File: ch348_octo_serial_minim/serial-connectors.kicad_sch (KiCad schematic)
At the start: 2 parts, among them J15 Conn_01x04

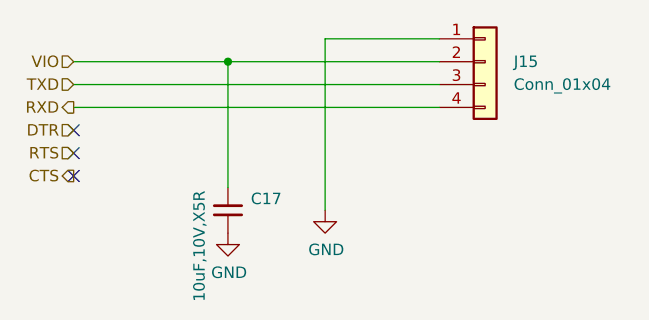
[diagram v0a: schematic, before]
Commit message: ch348_octo_serial_minim: jan2023 rev ready for production
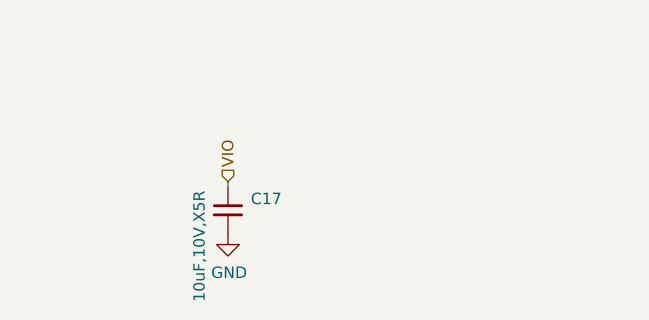
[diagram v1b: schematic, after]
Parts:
- removed J15: Conn_01x04, tom-connectors:PinHeader_1x04_P2.54mm_Vertical, symbol tom-connectors:Conn_01x04
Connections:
- no-connect marks 3 -> 0
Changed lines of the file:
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@@
 (kicad_sch (version 20211123) (generator eeschema)
   (paper "A4")
-  (junction (at 67.31 69.215) (diameter 0) (color 0 0 0 0)
-  )
-  (no_connect (at 50.165 76.835))
-  (no_connect (at 50.165 79.375))
-  (no_connect (at 50.165 81.915))
-  (wire (pts (xy 50.165 74.295) (xy 90.805 74.295))
-    (stroke (width 0) (type default) (color 0 0 0 0))
-  )
-  (wire (pts (xy 78.105 66.675) (xy 78.105 85.725))
-    (stroke (width 0) (type default) (color 0 0 0 0))
-  )
-  (wire (pts (xy 67.31 69.215) (xy 90.805 69.215))
-    (stroke (width 0) (type default) (color 0 0 0 0))
-  )
-  (wire (pts (xy 50.165 71.755) (xy 90.805 71.755))
-    (stroke (width 0) (type default) (color 0 0 0 0))
-  )
-  (wire (pts (xy 50.165 69.215) (xy 67.31 69.215))
-    (stroke (width 0) (type default) (color 0 0 0 0))
-  )
-  (wire (pts (xy 67.31 69.215) (xy 67.31 83.185))
-    (stroke (width 0) (type default) (color 0 0 0 0))
-  )
-  (wire (pts (xy 90.805 66.675) (xy 78.105 66.675))
+  (wire (pts (xy 67.31 82.55) (xy 67.31 83.185))
     (stroke (width 0) (type default) (color 0 0 0 0))
   )
@@
     )
   )
-  (hierarchical_label "TXD" (shape input) (at 50.165 71.755 180)
-    (effects (font (size 1.27 1.27)) (justify right))
-  )
-  (hierarchical_label "VIO" (shape input) (at 50.165 69.215 180)
-    (effects (font (size 1.27 1.27)) (justify right))
-  )
-  (hierarchical_label "DTR" (shape input) (at 50.165 76.835 180)
-    (effects (font (size 1.27 1.27)) (justify right))
-  )
-  (hierarchical_label "CTS" (shape output) (at 50.165 81.915 180)
-    (effects (font (size 1.27 1.27)) (justify right))
-  )
-  (hierarchical_label "RXD" (shape output) (at 50.165 74.295 180)
-    (effects (font (size 1.27 1.27)) (justify right))
-  )
-  (hierarchical_label "RTS" (shape input) (at 50.165 79.375 180)
-    (effects (font (size 1.27 1.27)) (justify right))
-  )
-  (symbol (lib_id "tom-connectors:Conn_01x04") (at 95.885 69.215 0) (unit 1)
-    (in_bom yes) (on_board yes) (fields_autoplaced)
-    (property "Reference" "J15" (id 0) (at 99.06 69.2149 0)
-      (effects (font (size 1.27 1.27)) (justify left))
-    )
-    (property "Value" "Conn_01x04" (id 1) (at 99.06 71.7549 0)
-      (effects (font (size 1.27 1.27)) (justify left))
-    )
-    (property "Footprint" "tom-connectors:PinHeader_1x04_P2.54mm_Vertical" (id 2) (at 95.885 69.215 0)
-      (effects (font (size 1.27 1.27)) hide)
-    )
-    (property "Datasheet" "~" (id 3) (at 95.885 69.215 0)
-      (effects (font (size 1.27 1.27)) hide)
-    )
-    (property "LCSC" "C725908" (id 4) (at 95.885 69.215 0)
-      (effects (font (size 1.27 1.27)) hide)
-    )
-    (pin "1")
-    (pin "2")
-    (pin "3")
-    (pin "4")
-  )
-  (symbol (lib_id "power:GND") (at 78.105 85.725 0) (unit 1)
-    (in_bom yes) (on_board yes)
-    (property "Reference" "#PWR052" (id 0) (at 78.105 92.075 0)
-      (effects (font (size 1.27 1.27)) hide)
-    )
-    (property "Value" "GND" (id 1) (at 78.232 90.1192 0))
-    (property "Footprint" "" (id 2) (at 78.105 85.725 0)
-      (effects (font (size 1.27 1.27)) hide)
-    )
-    (property "Datasheet" "" (id 3) (at 78.105 85.725 0)
-      (effects (font (size 1.27 1.27)) hide)
-    )
-    (pin "1")
+  (hierarchical_label "VIO" (shape input) (at 67.31 82.55 90)
+    (effects (font (size 1.27 1.27)) (justify left))
   )
   (symbol (lib_id "jlcpcb-basic-capacitor-0603:10uF,10V,X5R ") (at 67.31 85.725 0) (unit 1)
